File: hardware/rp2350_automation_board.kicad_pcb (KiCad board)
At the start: 2 copper layers, 1 part, among them IC1 SC1509

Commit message: XTR117 Output
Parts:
- removed IC1: SC1509, Samacsys:QFN40P700X700X90-61N-D
- added Q1: FCX690BTA, EasyEDA:SOT-89-3_L4.5-W2.5-P1.50-LS4.2-BR, F.Cu at (84.4, 41.5)
- added U1: XTR117AIDGKR, EasyEDA:VSSOP-8_L3.0-W3.0-P0.65-LS5.0-BL, F.Cu at (97.5, 32.0)
- added U2: ISO7041FDBQR, EasyEDA:SSOP-16_L4.9-W3.9-P0.64-LS6.0-BL, F.Cu at (114.0, 41.5)
- added U3: Pico, MCU_RaspberryPi_and_Boards:RPi_Pico_SMD_TH, F.Cu at (45.6, 85.4)
- added U4: DAC60501MDGSR, EasyEDA:VSSOP-10_L3.0-W3.0-P0.50-LS4.9-BL, F.Cu at (63.0, 33.6)
- added U5: INA219AIDCNR, EasyEDA:SOT-23-8_L3.0-W1.7-P0.65-LS2.8-BR, F.Cu at (131.0, 57.5)

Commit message: Almost everything
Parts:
- added Q2: NTF2955T1G, EasyEDA:SOT-223-4_L6.5-W3.5-P2.30-LS7.0-BR, F.Cu at (198.9, 65.3)
- added Q3: MMBT2907ALT1G, EasyEDA:SOT-23-3_L2.9-W1.3-P1.90-LS2.4-BR, F.Cu at (184.4, 80.9)
- added U10: REF3040AIDBZR, EasyEDA:SOT-23-3_L2.9-W1.6-P1.90-LS2.8-BR, F.Cu at (205.7, 63.5)
- added U11: KF301-5.0-2P, EasyEDA:CONN-TH_P5.00_KF301-5.0-2P, F.Cu at (188.0, 66.0)
- added U12: TLV9301IDBVR, EasyEDA:SOT-23-5_L3.0-W1.7-P0.95-LS2.8-BR, F.Cu at (184.7, 76.7)
- added U13: MAX3485AEASA+T, EasyEDA:SO-8_L4.9-W3.9-P1.27-LS5.9-BL, F.Cu at (185.9, 99.5)
- added U14: KF301-5.0-2P, EasyEDA:CONN-TH_P5.00_KF301-5.0-2P, F.Cu at (188.0, 90.9)
- added U15: KF301-5.0-2P, EasyEDA:CONN-TH_P5.00_KF301-5.0-2P, F.Cu at (127.9, 61.8)
- added U16: KF301-5.0-2P, EasyEDA:CONN-TH_P5.00_KF301-5.0-2P, F.Cu at (127.9, 70.9)
- added U17: KF301-5.0-2P, EasyEDA:CONN-TH_P5.00_KF301-5.0-2P, F.Cu at (106.0, 86.2)
- added U18: KF301-5.0-2P, EasyEDA:CONN-TH_P5.00_KF301-5.0-2P, F.Cu at (107.5, 98.8)
- added U19: KF301-5.0-2P, EasyEDA:CONN-TH_P5.00_KF301-5.0-2P, F.Cu at (107.5, 107.9)
- added U20: KF301-5.0-2P, EasyEDA:CONN-TH_P5.00_KF301-5.0-2P, F.Cu at (107.5, 116.9)
- added U6: TLV9301IDBVR, EasyEDA:SOT-23-5_L3.0-W1.7-P0.95-LS2.8-BR, F.Cu at (184.7, 72.5)
- added U7: INA226AIDGSR, EasyEDA:MSOP-10_L3.0-W3.0-P0.50-LS5.0-BL, F.Cu at (201.3, 79.6)
- added U8: DAC60501MDGSR, EasyEDA:VSSOP-10_L3.0-W3.0-P0.50-LS4.9-BL, F.Cu at (200.9, 72.7)
- added U9: DAC60501MDGSR, EasyEDA:VSSOP-10_L3.0-W3.0-P0.50-LS4.9-BL, F.Cu at (205.2, 72.7)
- U5: value INA219AIDCNR -> XTR111AIDGQR; footprint EasyEDA:SOT-23-8_L3.0-W1.7-P0.65-LS2.8-BR -> EasyEDA:MSOP-10_L3.0-W3.0-P0.50-LS5.0-BL-EP
- moved U4 139.1 mm to (196.6, 72.7)
- moved Q1 113.7 mm to (190.8, 81.4)
- moved U1 110.1 mm to (196.7, 79.6)
- moved U2 83.4 mm to (190.7, 74.4)
- moved U5 78.1 mm to (205.9, 79.6)
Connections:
- U1 pad 2: unconnected-(U1-IIN-Pad2) -> Net-(U1-IIN)
- U2 pad 1: unconnected-(U2-VCC1-Pad1) -> +5V_MCU
- U2 pad 10: unconnected-(U2-EN2-Pad10) -> GND_XTR
- U2 pad 12: unconnected-(U2-OUTC-Pad12) -> Net-(U2-OUTC)
- U2 pad 13: unconnected-(U2-OUTB-Pad13) -> Net-(U2-OUTB)
- U2 pad 14: unconnected-(U2-OUTA-Pad14) -> Net-(U2-OUTA)
- U2 pad 16: unconnected-(U2-VCC2-Pad16) -> 5V_XTR
- U2 pad 3: unconnected-(U2-INA-Pad3) -> SPI0_CLK
- U2 pad 4: unconnected-(U2-INB-Pad4) -> SPI0_CS
- U2 pad 5: unconnected-(U2-INC-Pad5) -> SPI0_MOSI
- U2 pad 6: unconnected-(U2-OUTD-Pad6) -> SPI0_MISO
- U2 pad 7: unconnected-(U2-EN1-Pad7) -> GND_MCU
- U2 pad 8: unconnected-(U2-GND1-Pad8) -> GND_MCU
- U2 pad 9: unconnected-(U2-GND2-Pad9) -> GND_XTR
- U3 pad 21: SPI0_MISO -> UART_TX
- U3 pad 22: SPI0_CS -> UART_RX
- U3 pad 24: SPI0_CLK -> RS485_MODE
- U3 pad 25: SPI0_MOSI -> unconnected-(U3-GPIO19-Pad25)
- U3 pad 26: unconnected-(U3-GPIO20-Pad26) -> SDA
- U3 pad 27: unconnected-(U3-GPIO21-Pad27) -> SCL
- U3 pad 31: unconnected-(U3-GPIO26_ADC0-Pad31) -> ADC0
- U3 pad 36: +3V3_MCU -> +3V3
- U3 pad 39: unconnected-(U3-VSYS-Pad39) -> VSYS
- U3 pad 40: +5V_MCU -> unconnected-(U3-VBUS-Pad40)_1
- U4 pad 1: unconnected-(U4-VDD-Pad1) -> 5V_XTR
- U4 pad 2: unconnected-(U4-VOUT-Pad2) -> Net-(U4-VOUT)
- U4 pad 4: unconnected-(U4-AGND-Pad4) -> GND_XTR
- U4 pad 5: unconnected-(U4-SPI2C-Pad5) -> Net-(U4-SPI2C)
- U4 pad 6: unconnected-(U4-SCLK/SCL-Pad6) -> Net-(U2-OUTA)
- U4 pad 7: unconnected-(U4-~{SYNC}/A0-Pad7) -> Net-(U2-OUTB)
- U4 pad 8: unconnected-(U4-SDIN/SDA-Pad8) -> Net-(U2-OUTC)
- U5 pad 1: unconnected-(U5-IN+-Pad1) -> +12V
- U5 pad 2: unconnected-(U5-IN--Pad2) -> Net-(Q3-E)
- U5 pad 3: unconnected-(U5-GND-Pad3) -> Net-(Q3-C)
- U5 pad 4: unconnected-(U5-VS-Pad4) -> Net-(U5-REGS)
- U5 pad 5: unconnected-(U5-SCL-Pad5) -> Net-(U5-REGF)
- U5 pad 6: unconnected-(U5-SDA-Pad6) -> Net-(U5-VIN)
- U5 pad 7: unconnected-(U5-A0-Pad7) -> Net-(U5-SET)

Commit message: Board complete
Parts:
- removed U16, U17, U18, U19, U20: KF301-5.0-2P, EasyEDA:CONN-TH_P5.00_KF301-5.0-2P
- removed U2: ISO7041FDBQR, EasyEDA:SSOP-16_L4.9-W3.9-P0.64-LS6.0-BL
- removed U3: Pico, MCU_RaspberryPi_and_Boards:RPi_Pico_SMD_TH
- added C1: 2.2uF, Capacitor_SMD:C_1206_3216Metric_Pad1.33x1.80mm_HandSolder, F.Cu at (94.5, 104.9)
- added C10: 10uF, Capacitor_SMD:C_1206_3216Metric_Pad1.33x1.80mm_HandSolder, F.Cu at (147.9, 51.8)
- added C11: 1uF, Capacitor_SMD:C_1206_3216Metric_Pad1.33x1.80mm_HandSolder, F.Cu at (135.8, 81.2)
- added C12: 150nF, Capacitor_SMD:C_1206_3216Metric_Pad1.33x1.80mm_HandSolder, F.Cu at (141.4, 80.0)
- added C13: 0.1uF, Capacitor_SMD:C_1206_3216Metric_Pad1.33x1.80mm_HandSolder, F.Cu at (149.2, 36.9)
- added C14: 0.1uF, Capacitor_SMD:C_1206_3216Metric_Pad1.33x1.80mm_HandSolder, F.Cu at (156.7, 49.0)
- added C15: 470nF, Capacitor_SMD:C_1206_3216Metric_Pad1.33x1.80mm_HandSolder, F.Cu at (157.5, 82.0)
- added C16: 10nF, Capacitor_SMD:C_1206_3216Metric_Pad1.33x1.80mm_HandSolder, F.Cu at (153.8, 77.7)
- added C17: C, Capacitor_SMD:C_1206_3216Metric_Pad1.33x1.80mm_HandSolder, F.Cu at (152.1, 94.5)
- added C18: 1nF, Capacitor_SMD:C_1206_3216Metric_Pad1.33x1.80mm_HandSolder, F.Cu at (135.9, 78.5)
- added C19: 0.1uF, Capacitor_SMD:C_1206_3216Metric_Pad1.33x1.80mm_HandSolder, F.Cu at (154.9, 89.0)
- added C2: 2.2uF, Capacitor_SMD:C_1206_3216Metric_Pad1.33x1.80mm_HandSolder, F.Cu at (66.9, 104.8)
- added C3: 0.1uF, Capacitor_SMD:C_1206_3216Metric_Pad1.33x1.80mm_HandSolder, F.Cu at (90.9, 110.6)
- added C4: 0.1uF, Capacitor_SMD:C_1206_3216Metric_Pad1.33x1.80mm_HandSolder, F.Cu at (63.5, 110.4)
- added C5: 22uF, Capacitor_SMD:C_1206_3216Metric_Pad1.33x1.80mm_HandSolder, F.Cu at (104.5, 113.3)
- added C6: 10uF, Capacitor_SMD:C_1206_3216Metric_Pad1.33x1.80mm_HandSolder, F.Cu at (73.3, 111.2)
- added C7: 22uF, Capacitor_SMD:C_1206_3216Metric_Pad1.33x1.80mm_HandSolder, F.Cu at (104.5, 115.7)
- added C8: 10uF, Capacitor_SMD:C_1206_3216Metric_Pad1.33x1.80mm_HandSolder, F.Cu at (73.3, 114.2)
- added C9: 10uF, Capacitor_SMD:C_1206_3216Metric_Pad1.33x1.80mm_HandSolder, F.Cu at (135.8, 84.0)
- added D1: MBR230S1F-7, Samacsys:SODFL3518X115N, F.Cu at (118.9, 32.4)
- added D2: 1N4148W, Samacsys:SODFL3816X120N, F.Cu at (77.9, 38.4)
- added D3: 1N4148W, Samacsys:SODFL3816X120N, F.Cu at (77.9, 46.7)
- added D4: 1N4007W-T, Samacsys:SODFL3818X130N, F.Cu at (59.7, 71.8)
- added D5: 1N4007W-T, Samacsys:SODFL3818X130N, F.Cu at (68.8, 71.8)
- added D6: 1N4148W, Samacsys:SODFL3816X120N, F.Cu at (77.9, 30.0)
- added D7: 1N4007W-T, Samacsys:SODFL3818X130N, F.Cu at (77.9, 71.8)
- added D8: CDSOT23-SM712, Samacsys:SOT95P230X117-3N, F.Cu at (162.3, 99.8)
- added IC1: DAC7562SDGSR, Samacsys:SOP50P490X110-10N, F.Cu at (142.0, 77.0)
- added IC2: SN65HVD75DGKR, Samacsys:SOP65P490X110-8N, F.Cu at (149.9, 99.8)
- added IC3: LMR51420XFDDCR, Samacsys:SOT95P280X110-6N, F.Cu at (94.9, 108.1)
- added J1: PH1-20-UA, Samacsys:HDRV20W64P0X254_1X20_5080X249X886P, F.Cu at (97.3, 24.6)
- added J10: TB007-508-02BE, Samacsys:TB00750802BE, F.Cu at (171.5, 53.3)
- added J11: TB007-508-02BE, Samacsys:TB00750802BE, F.Cu at (171.5, 25.4)
- added J12: TB007-508-02BE, Samacsys:TB00750802BE, F.Cu at (171.5, 66.0)
- added J13: 39880-0303, Samacsys:398800303, F.Cu at (172.7, 97.4)
- added J14: TB006-508-03BE, Samacsys:TB00650803BE, F.Cu at (46.7, 89.9)
- added J2: PH1-20-UA, Samacsys:HDRV20W64P0X254_1X20_5080X249X886P, F.Cu at (133.4, 24.7)
- added J3: TB006-508-03BE, Samacsys:TB00650803BE, F.Cu at (125.3, 117.8)
- added J4: TB006-508-03BE, Samacsys:TB00650803BE, F.Cu at (132.8, 117.8)
- added J5: TB007-508-02BE, Samacsys:TB00750802BE, F.Cu at (47.5, 98.7)
- added J7: TB006-508-03BE, Samacsys:TB00650803BE, F.Cu at (46.7, 37.8)
- added J9: TB007-508-02BE, Samacsys:TB00750802BE, F.Cu at (171.5, 38.1)
- added L1: 22uH, Samacsys:INDPM7070X480N, F.Cu at (103.2, 108.1)
- added L2: 4.7uH, Samacsys:INDC3225X120N, F.Cu at (73.7, 107.8)
- added L3: 4.7uH, Samacsys:INDC3225X120N, F.Cu at (135.9, 87.2)
- added L4: 1uH, Samacsys:LQM31PN1R0M00L, F.Cu at (147.8, 55.8)
- added PS1: LMR51420YFDDCR, Samacsys:SOT95P280X110-6N, F.Cu at (67.2, 107.8)
- added Q4: MMBT2907ALT1G, EasyEDA:SOT-23-3_L2.9-W1.3-P1.90-LS2.4-BR, F.Cu at (161.5, 84.3)
- added Q5: BSP171PH6327XTSA1, EasyEDA:SOT-223-4_L6.5-W3.5-P2.30-LS7.0-BR, F.Cu at (158.8, 72.9)
- added R1: 100k, Resistor_SMD:R_1206_3216Metric_Pad1.30x1.75mm_HandSolder, F.Cu at (84.5, 108.6)
- added R10: 10k, Resistor_SMD:R_1206_3216Metric_Pad1.30x1.75mm_HandSolder, F.Cu at (89.1, 42.7)
- added R11: 20k, Resistor_SMD:R_1206_3216Metric_Pad1.30x1.75mm_HandSolder, F.Cu at (78.9, 96.8)
- added R12: 20k, Resistor_SMD:R_1206_3216Metric_Pad1.30x1.75mm_HandSolder, F.Cu at (79.0, 82.3)
- added R13: 3.3k, Resistor_SMD:R_1206_3216Metric_Pad1.30x1.75mm_HandSolder, F.Cu at (55.1, 91.7)
- added R14: 3.3k, Resistor_SMD:R_1206_3216Metric_Pad1.30x1.75mm_HandSolder, F.Cu at (54.8, 77.2)
- added R15: 330, Resistor_SMD:R_1206_3216Metric_Pad1.30x1.75mm_HandSolder, F.Cu at (88.9, 28.4)
- added R16: 10k, Resistor_SMD:R_1206_3216Metric_Pad1.30x1.75mm_HandSolder, F.Cu at (88.9, 26.0)
- added R17: 10k, Resistor_SMD:R_1206_3216Metric_Pad1.30x1.75mm_HandSolder, F.Cu at (78.9, 87.4)
- added R18: 20k, Resistor_SMD:R_1206_3216Metric_Pad1.30x1.75mm_HandSolder, F.Cu at (78.9, 89.9)
- added R19: 3.3k, Resistor_SMD:R_1206_3216Metric_Pad1.30x1.75mm_HandSolder, F.Cu at (55.0, 84.8)
- added R2: 5.23k, Resistor_SMD:R_1206_3216Metric_Pad1.30x1.75mm_HandSolder, F.Cu at (87.8, 108.6)
- added R20: 100k, Resistor_SMD:R_1206_3216Metric_Pad1.30x1.75mm_HandSolder, F.Cu at (153.4, 41.4)
- added R21: 10k, Resistor_SMD:R_1206_3216Metric_Pad1.30x1.75mm_HandSolder, F.Cu at (155.7, 57.7)
- added R22: 56k, Resistor_SMD:R_1206_3216Metric_Pad1.30x1.75mm_HandSolder, F.Cu at (145.5, 41.4)
- added R23: 24k, Resistor_SMD:R_1206_3216Metric_Pad1.30x1.75mm_HandSolder, F.Cu at (145.5, 34.5)
- added R24: 30k, Resistor_SMD:R_1206_3216Metric_Pad1.30x1.75mm_HandSolder, F.Cu at (160.8, 54.9)
- added R25: 1.25k, Resistor_SMD:R_1206_3216Metric_Pad1.30x1.75mm_HandSolder, F.Cu at (146.9, 84.3)
- added R26: 10k, Resistor_SMD:R_1206_3216Metric_Pad1.30x1.75mm_HandSolder, F.Cu at (149.6, 85.2)
- added R27: 0R, Resistor_SMD:R_1206_3216Metric_Pad1.30x1.75mm_HandSolder, F.Cu at (148.3, 80.0)
- added R28: 250R, Resistor_SMD:R_1206_3216Metric_Pad1.30x1.75mm_HandSolder, F.Cu at (150.6, 25.4)
- added R29: 22k, Resistor_SMD:R_1206_3216Metric_Pad1.30x1.75mm_HandSolder, F.Cu at (150.6, 29.2)
- added R3: 100k, Resistor_SMD:R_1206_3216Metric_Pad1.30x1.75mm_HandSolder, F.Cu at (56.8, 108.4)
- added R30: 33k, Resistor_SMD:R_1206_3216Metric_Pad1.30x1.75mm_HandSolder, F.Cu at (145.5, 27.7)
- added R31: 15, Resistor_SMD:R_1206_3216Metric_Pad1.30x1.75mm_HandSolder, F.Cu at (160.7, 87.3)
- added R32: 15, Resistor_SMD:R_1206_3216Metric_Pad1.30x1.75mm_HandSolder, F.Cu at (151.7, 71.4)
- added R33: 10k, Resistor_SMD:R_1206_3216Metric_Pad1.30x1.75mm_HandSolder, F.Cu at (145.0, 97.2)
- added R34: 10k, Resistor_SMD:R_1206_3216Metric_Pad1.30x1.75mm_HandSolder, F.Cu at (149.6, 95.0)
- added R35: 120R, Resistor_SMD:R_1206_3216Metric_Pad1.30x1.75mm_HandSolder, F.Cu at (157.0, 99.8)
- added R4: 13.7k, Resistor_SMD:R_1206_3216Metric_Pad1.30x1.75mm_HandSolder, F.Cu at (59.9, 108.4)
- added R5: 330, Resistor_SMD:R_1206_3216Metric_Pad1.30x1.75mm_HandSolder, F.Cu at (88.9, 36.8)
- added R6: 10k, Resistor_SMD:R_1206_3216Metric_Pad1.30x1.75mm_HandSolder, F.Cu at (78.9, 94.2)
- added R7: 10k, Resistor_SMD:R_1206_3216Metric_Pad1.30x1.75mm_HandSolder, F.Cu at (79.0, 79.8)
- added R8: 330, Resistor_SMD:R_1206_3216Metric_Pad1.30x1.75mm_HandSolder, F.Cu at (89.1, 45.2)
- added R9: 10k, Resistor_SMD:R_1206_3216Metric_Pad1.30x1.75mm_HandSolder, F.Cu at (88.9, 34.3)
- added RLY1: G5NB-1A-E-DC12, EasyEDA:RELAY-TH_G5NB-1A-E-DCXX, F.Cu at (63.0, 44.2)
- added RLY2: G5NB-1A-E-DC12, EasyEDA:RELAY-TH_G5NB-1A-E-DCXX, F.Cu at (63.0, 36.0)
- added RLY3: G5NB-1A-E-DC12, EasyEDA:RELAY-TH_G5NB-1A-E-DCXX, F.Cu at (63.0, 27.8)
- added TP1: TP_+12V, TestPoint:TestPoint_THTPad_2.0x2.0mm_Drill1.0mm, F.Cu at (103.2, 102.2)
- added TP10: TP_AI_0-10V, TestPoint:TestPoint_THTPad_2.0x2.0mm_Drill1.0mm, F.Cu at (158.1, 40.8)
- added TP11: TP_ADC1, TestPoint:TestPoint_THTPad_2.0x2.0mm_Drill1.0mm, F.Cu at (138.2, 29.1)
- added TP2: GND_TP, TestPoint:TestPoint_THTPad_D2.0mm_Drill1.0mm, F.Cu at (48.0, 116.6)
- added TP3: TP_+5V, TestPoint:TestPoint_THTPad_2.0x2.0mm_Drill1.0mm, F.Cu at (71.9, 102.4)
- added TP4: GND_TP, TestPoint:TestPoint_THTPad_D2.0mm_Drill1.0mm, F.Cu at (141.1, 108.3)
- added TP5: TP_+24V, TestPoint:TestPoint_THTPad_2.0x2.0mm_Drill1.0mm, F.Cu at (59.4, 102.6)
- added TP6: GND_TP, TestPoint:TestPoint_THTPad_D2.0mm_Drill1.0mm, F.Cu at (134.7, 108.3)
- added TP7: GND_TP, TestPoint:TestPoint_THTPad_D2.0mm_Drill1.0mm, F.Cu at (158.2, 33.7)
- added TP8: TP_AO_0-10V, TestPoint:TestPoint_THTPad_2.0x2.0mm_Drill1.0mm, F.Cu at (160.8, 50.4)
- added TP9: TP_ADC0, TestPoint:TestPoint_THTPad_2.0x2.0mm_Drill1.0mm, F.Cu at (140.8, 49.9)
- Q1: value FCX690BTA -> 2N7002; footprint EasyEDA:SOT-89-3_L4.5-W2.5-P1.50-LS4.2-BR -> EasyEDA:SOT-23-3_L2.9-W1.3-P1.90-LS2.4-BR
- Q2: value NTF2955T1G -> 2N7002; footprint EasyEDA:SOT-223-4_L6.5-W3.5-P2.30-LS7.0-BR -> EasyEDA:SOT-23-3_L2.9-W1.3-P1.90-LS2.4-BR
- Q3: value MMBT2907ALT1G -> 2N7002
- U1: value XTR117AIDGKR -> Pico; footprint EasyEDA:VSSOP-8_L3.0-W3.0-P0.65-LS5.0-BL -> RP-Pico Libraries:RPi_Pico_SMD_TH
- U10: value REF3040AIDBZR -> FUSE_C; footprint EasyEDA:SOT-23-3_L2.9-W1.6-P1.90-LS2.8-BR -> Samacsys:01110501Z
- U11: value KF301-5.0-2P -> LTV-814S-TA1; footprint EasyEDA:CONN-TH_P5.00_KF301-5.0-2P -> EasyEDA:SMD-4_L4.6-W6.5-P2.54-LS10.2-BL
- U12: value TLV9301IDBVR -> FUSE_C; footprint EasyEDA:SOT-23-5_L3.0-W1.7-P0.95-LS2.8-BR -> Samacsys:01110501Z
- U13: value MAX3485AEASA+T -> TLV9301IDBVR; footprint EasyEDA:SO-8_L4.9-W3.9-P1.27-LS5.9-BL -> EasyEDA:SOT-23-5_L3.0-W1.7-P0.95-LS2.8-BR
- U14: value KF301-5.0-2P -> TLV9301IDBVR; footprint EasyEDA:CONN-TH_P5.00_KF301-5.0-2P -> EasyEDA:SOT-23-5_L3.0-W1.7-P0.95-LS2.8-BR
- U15: value KF301-5.0-2P -> XTR111AIDGQR; footprint EasyEDA:CONN-TH_P5.00_KF301-5.0-2P -> EasyEDA:MSOP-10_L3.0-W3.0-P0.50-LS5.0-BL-EP
- U4, U8, U9: value DAC60501MDGSR -> FUSE_C; footprint EasyEDA:VSSOP-10_L3.0-W3.0-P0.50-LS4.9-BL -> Samacsys:01110501Z
- U5: value XTR111AIDGQR -> FUSE_C; footprint EasyEDA:MSOP-10_L3.0-W3.0-P0.50-LS5.0-BL-EP -> Samacsys:01110501Z
- U6: value TLV9301IDBVR -> LTV-814S-TA1; footprint EasyEDA:SOT-23-5_L3.0-W1.7-P0.95-LS2.8-BR -> EasyEDA:SMD-4_L4.6-W6.5-P2.54-LS10.2-BL
- U7: value INA226AIDGSR -> LTV-814S-TA1; footprint EasyEDA:MSOP-10_L3.0-W3.0-P0.50-LS5.0-BL -> EasyEDA:SMD-4_L4.6-W6.5-P2.54-LS10.2-BL
- moved U8 146.3 mm to (54.7, 66.0), turned to 90 degrees
- moved U9 141.5 mm to (63.8, 66.0), turned to 90 degrees
- moved U5 140.0 mm to (68.8, 51.6), turned to -90 degrees
- moved U4 138.5 mm to (59.7, 51.6), turned to -90 degrees
- moved U7 135.5 mm to (65.8, 78.5), turned to -90 degrees
- moved U10 128.4 mm to (77.9, 51.6), turned to -90 degrees
- moved U11 123.9 mm to (65.7, 86.1), turned to -90 degrees
- moved U6 120.7 mm to (65.7, 93.0), turned to -90 degrees
- moved Q2 117.2 mm to (83.5, 44.3)
- moved Q1 116.5 mm to (83.5, 35.9)
- moved Q3 114.1 mm to (83.5, 27.6)
- moved U12 112.3 mm to (72.9, 66.0), turned to 90 degrees
- moved U1 87.0 mm to (115.4, 48.8)
- moved U13 68.0 mm to (150.1, 41.7), turned to -90 degrees
- moved U14 49.7 mm to (155.4, 53.4), turned to 180 degrees
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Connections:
- Q1 pad 1: Net-(Q1-B) -> Net-(Q1-G)
- Q1 pad 2: AO_4-20mA_IN -> GND
- Q1 pad 3: Net-(Q1-E) -> Net-(D2-A)
- Q2 pad 2: unconnected-(Q2-D-Pad2) -> GND
- Q3 pad 1: Net-(Q2-G) -> Net-(Q3-G)
- Q3 pad 2: Net-(Q3-E) -> GND
- Q3 pad 3: Net-(Q3-C) -> Net-(D6-A)
- U1 pad 1: unconnected-(U1-NC-Pad1) -> Net-(U1-GPIO0)
- U1 pad 3: GND_XTR -> GND
- U1 pad 4: AO_4-20mA_OUT -> DOUT_1
- U1 pad 5: Net-(Q1-E) -> DOUT_2
- U1 pad 6: Net-(Q1-B) -> DOUT_3
- U1 pad 7: AO_4-20mA_IN -> DIN_1
- U1 pad 8: 5V_XTR -> GND
- U10 pad 1: +12V -> Net-(RLY3-Pad3)
- U10 pad 2: Net-(U10-OUT) -> Net-(RLY3-Pad3)
- U11 pad 1: unconnected-(U11-Pad1) -> Net-(R19-Pad2)
- U11 pad 2: unconnected-(U11-Pad2) -> GND
- U12 pad 1: Net-(U12--IN) -> Net-(D7-K)
- U12 pad 2: AI_4-20mA_GND -> Net-(D7-K)
- U13 pad 1: UART_RX -> Net-(U13--IN)
- U13 pad 2: RS485_MODE -> GND
- U13 pad 3: RS485_MODE -> /Analog IO/AI_0-10V_IN
- U13 pad 4: UART_TX -> Net-(U13--IN)
- U13 pad 5: AI_4-20mA_GND -> +12V_LPF_OP
- U14 pad 1: RS485_B -> /Analog IO/AO_0-10V
- U14 pad 2: RS485_A -> GND
- U15 pad 1: +12V -> +24V
- U15 pad 2: +12V -> Net-(Q4-E)
- U4 pad 1: 5V_XTR -> Net-(RLY1-Pad3)
- U4 pad 2: Net-(U4-VOUT) -> Net-(RLY1-Pad3)
- U5 pad 1: +12V -> Net-(RLY2-Pad3)
- U5 pad 2: Net-(Q3-E) -> Net-(RLY2-Pad3)
- U6 pad 1: AO_0-10V_OUT -> Net-(R13-Pad2)
- U6 pad 2: AI_4-20mA_GND -> GND
- U6 pad 3: Net-(U6-+IN) -> Net-(R6-Pad1)
- U6 pad 4: Net-(U6--IN) -> +5V
- U7 pad 1: AI_4-20mA_GND -> Net-(R14-Pad2)
- U7 pad 2: AI_4-20mA_GND -> GND
- U7 pad 3: unconnected-(U7-Alert-Pad3) -> Net-(R7-Pad1)
- U7 pad 4: SDA -> +5V
- U8 pad 1: +12V -> Net-(D4-K)
- U8 pad 2: Net-(U6-+IN) -> Net-(D4-K)
- U9 pad 1: +12V -> Net-(D5-K)
- U9 pad 2: Net-(U9-VOUT) -> Net-(D5-K)
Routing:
- net +5V: track 0.00 -> 239.2 mm, vias 0 -> 9
- net +24V: track 0.00 -> 226.6 mm, vias 0 -> 1
- net +12V: track 0.00 -> 211.4 mm, vias 0 -> 2
- net GND: track 0.00 -> 98.8 mm, vias 0 -> 57
- net UART_TX: track 0.00 -> 88.8 mm
- net +3V3: track 0.00 -> 85.2 mm, vias 0 -> 5
- net RS485_MODE: track 0.00 -> 84.9 mm
- net UART_RX: track 0.00 -> 83.5 mm
- net DIN_3: track 0.00 -> 65.5 mm
- net DIN_2: track 0.00 -> 62.2 mm
- net DIN_1: track 0.00 -> 61.2 mm
- net Net-(RLY3-Pad3): track 0.00 -> 49.1 mm
- net ADC1: track 0.00 -> 39.6 mm
- net +12V_LPF_OP: track 0.00 -> 36.3 mm
- net ADC0: track 0.00 -> 35.4 mm
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- added copper zone on F.Cu, net +24V
- added copper zone on F.Cu, net +3V3
- added copper zone on B.Cu, net GND
- added copper zone on F.Cu, net GND
- added copper zone on B.Cu, net Net-(C16-Pad2)
- added copper zone on F.Cu, net Net-(C16-Pad2)
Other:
- board outline added: 140 x 105 mm
- board text added: "+"
- board text added: "-"
- board text added: "0-10V"
- board text added: "4-20mA"
- board text added: "AI"
- board text added: "AO"
- board text added: "DI 24V"
- board text added: "DO 24V"
- board text added: "Igor Potyrala 272518 PWR 2025"
- board text added: "POWER 24V"

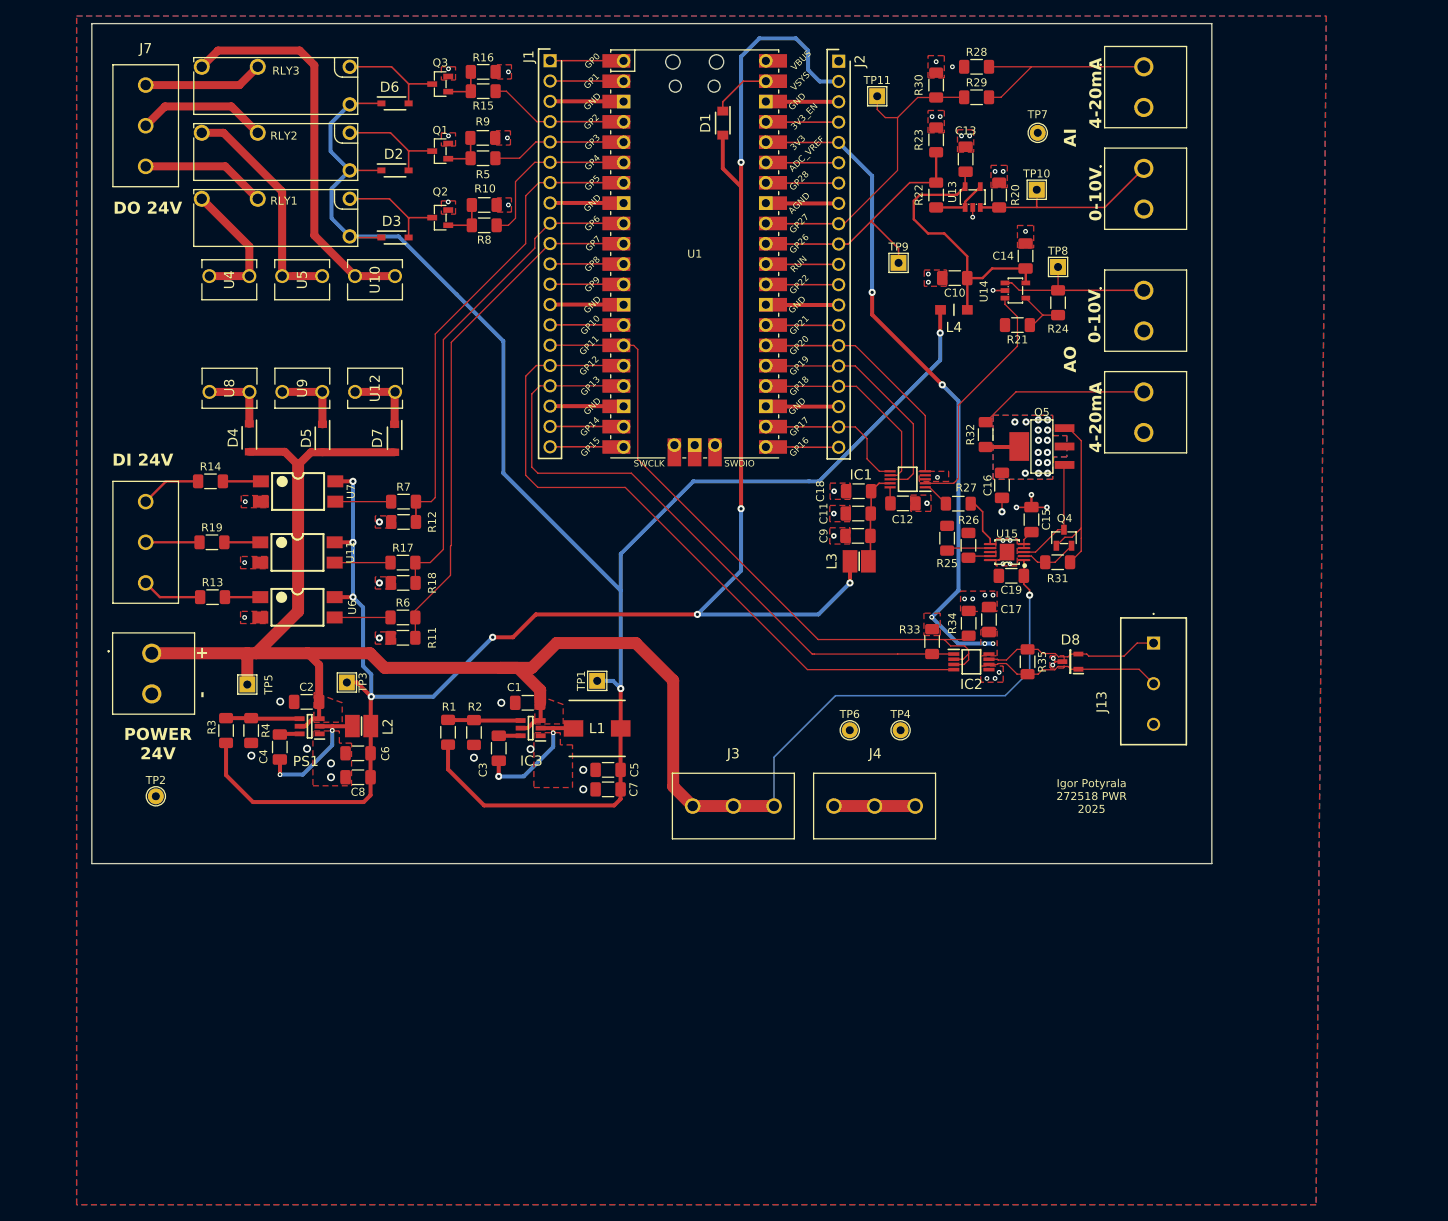
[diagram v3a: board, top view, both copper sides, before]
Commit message: LDAC added
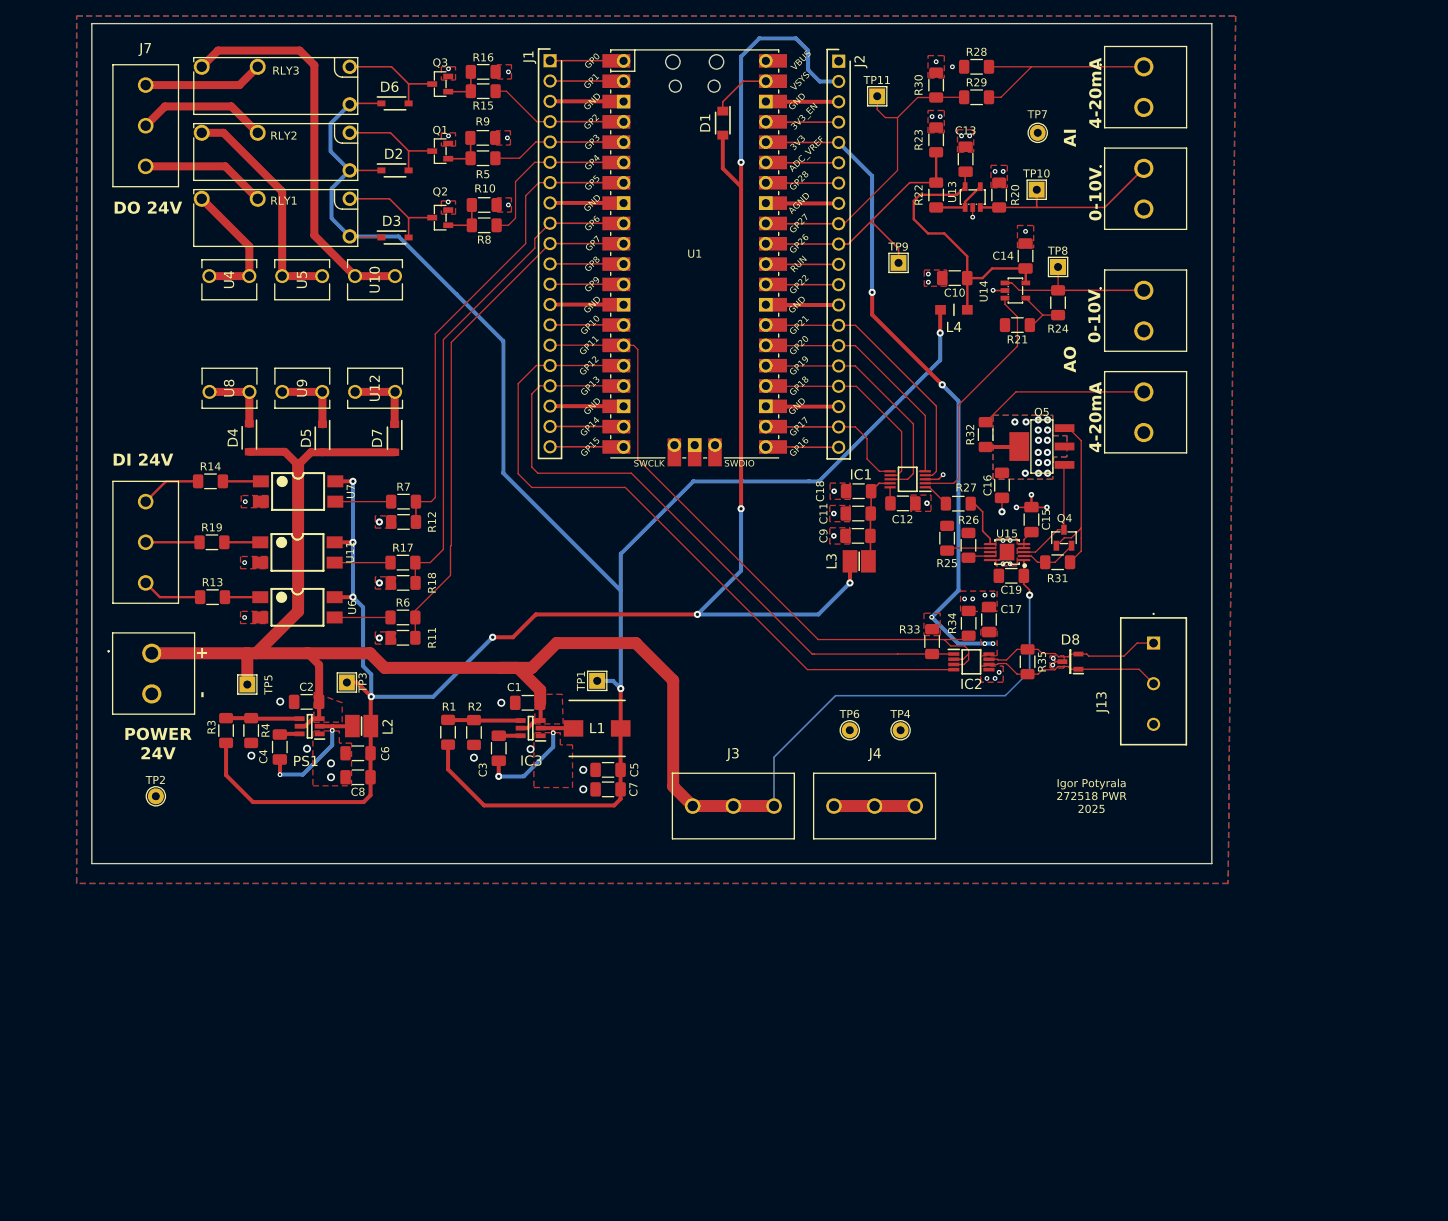
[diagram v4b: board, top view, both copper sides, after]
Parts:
- C17: value C -> 0.1uF
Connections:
- IC1 pad 4: GND -> DAC_LDAC
- J2 pad 14: Net-(U1-GPIO21) -> DAC_LDAC
- U1 pad 27: Net-(U1-GPIO21) -> DAC_LDAC
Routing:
- net DAC_LDAC: track 0.00 -> 35.3 mm
- net Net-(U1-GPIO21): track 9.14 -> 0.00 mm
- net GND: track 98.8 -> 101.2 mm
- net UART_TX: track 88.8 -> 90.0 mm

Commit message: Fixes
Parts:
- moved C5 12.8 mm to (104.6, 100.5)
- moved C7 12.8 mm to (104.6, 102.9)
- moved TP1 11.2 mm to (109.5, 111.5), turned to 180 degrees
- moved TP3 9.88 mm to (80.1, 107.9), turned to 0 degrees
- moved C8 9.51 mm to (73.3, 104.7)
- moved C6 8.98 mm to (73.3, 102.2)
- moved TP4 1.02 mm to (141.6, 109.2)
- moved TP6 1.02 mm to (135.3, 109.2)
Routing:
- net +12V: track 211.4 -> 222.3 mm
- net +5V: track 239.2 -> 240.4 mm
- net +24V: track 226.6 -> 225.8 mm
- net GND: track 101.2 -> 100.6 mm, vias 57 -> 68
- net Net-(C16-Pad2): vias 15 -> 4
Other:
- outline, holes or cut-outs redrawn
- board text added: "12V"
- board text added: "24V"
- board text added: "5V"
- board text added: "ADC0"
- board text added: "ADC1"
- board text added: "GND"

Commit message: Ordered
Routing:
- net GND: track 100.6 -> 93.6 mm, vias 68 -> 69
- net +24V: track 225.8 -> 228.5 mm
- net +5V: track 240.4 -> 243.0 mm
- net DAC_RESET: track 32.4 -> 31.2 mm
- net SPI0_MOSI: track 31.2 -> 30.0 mm
- net /Analog IO/AO_4-20mA: track 21.3 -> 22.3 mm
- net UART_TX: track 90.0 -> 89.3 mm
- net DAC_LDAC: track 35.3 -> 34.6 mm
